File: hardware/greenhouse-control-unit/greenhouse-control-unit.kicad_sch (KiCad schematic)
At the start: 76 parts, among them J1 Pluggable_Terminal_01x02, J10 Molex_KK-396_01x16, J10_LittleBuck1 Conn_01x01_Female, J11 Molex_KK-254_01x10, J11_LittleBuck1 Conn_01x01_Female, J12_BigBuck1 Conn_01x01_Female, J13_BigBuck1 Conn_01x01_Female, J14_LittleBuck1 Conn_01x01_Female, J15_LittleBuck1 Conn_01x01_Female, J2 Pluggable_Terminal_01x02, J3 Pluggable_Terminal_01x02, J4 Pluggable_Terminal_01x02, J5 Molex_KK-254_01x08, J6 Conn_01x10_Female, J6_BigBuck1 Conn_01x01_Female, J7 Conn_01x10_Female, J7_BigBuck1 Conn_01x01_Female, J8 Conn_01x15_Female, J9 Conn_01x15_Female, Q1 2N7000, Q10 IRLB8721PBF, Q11 IRLB8721PBF, Q2 2N7000, Q3 2N2222A, Q4 IRLB8721PBF, Q5 IRLB8721PBF, Q6 IRLB8721PBF, Q7 IRLB8721PBF, Q8 IRLB8721PBF, Q9 IRLB8721PBF, U1 74HC595, U2 74HC595

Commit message: Remove small buck
Also:
- Change source to 10V
- Use 5V for radios
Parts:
- removed J10_LittleBuck1, J11_LittleBuck1, J14_LittleBuck1, J15_LittleBuck1: Conn_01x01_Female, Connector_PinHeader_2.54mm:PinHeader_1x01_P2.54mm_Vertical, symbol Connector:Conn_01x01_Female
- D2: symbol Device:D_Schottky -> Device:D
- J12: renamed from J12_BigBuck1; value Conn_01x01_Female -> Buck_Conn_01x01_Female
- J13: renamed from J13_BigBuck1; value Conn_01x01_Female -> Buck_Conn_01x01_Female
- J6: renamed from J6_BigBuck1; value Conn_01x01_Female -> Buck_Conn_01x01_Female
- J7: renamed from J7_BigBuck1; value Conn_01x01_Female -> Buck_Conn_01x01_Female
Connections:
- net +5VA is gone; now on net +5V: D7.2 (A), J8.1 (Pin_1)
- net +3V3: no longer J?.2 (Pin_2), J?.4 (Pin_4)
- net +5V: now also J?.2 (Pin_2), J?.4 (Pin_4)
- net +12V renamed +10V
- net Batt+12V renamed Batt+10V
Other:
- note added: "Prototype TODO: -"
- note added: "Schematic TODO: - Disable SR when no input voltage (SR can draw power from inputs; i.e. MC) - Consider adding reverse voltage protection to power outputs - Check if PSU relay module has flyback diode"
- note removed: "Prototype TODO: - Add reverse voltage protection diode to battery relay - Check all R values - Test current on each SR out (max 20mA, limit 35mA) - Test current on SR VCC (max 70mA)"
- note removed: "Schematic TODO: - Disable SR when no input voltage (SR can draw power from inputs; i.e. MC) - Consider adding reverse voltage protection to power outputs - Check if PSU relay module has reverse voltage diode"
- moved on the sheet: H1, H2, H3, H4, H5, H6, J12, J13, J6, J7

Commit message: Reconfigured SR OE
Also:
- merged motor driver back into main schematic (to avoid needing global labels)
- renamed labels for headers/sockets
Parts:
- removed C1, C2: 0.01 μf, Capacitor_THT:C_Disc_D3.0mm_W1.6mm_P2.50mm, symbol Device:C
- removed D7: 1N4001, Diode_THT:D_DO-41_SOD81_P10.16mm_Horizontal, symbol Diode:1N4001
- removed J?: TX_PinHeader_1x04_P2.54mm, Connector_Molex:Molex_KK-254_AE-6410-08A_1x04_P2.54mm_Vertical, symbol Connector:Conn_01x04_Female
- removed J?: RX_PinHeader_1x04_P2.54mm, Connector_PinHeader_2.54mm:PinHeader_1x04_P2.54mm_Vertical, symbol Connector:Conn_01x04_Female
- removed Q?: 2N2222A, Package_TO_SOT_THT:TO-92_Inline, symbol Nick:2N2222A
- removed R9: 10k, Resistor_THT:R_Axial_DIN0204_L3.6mm_D1.6mm_P5.08mm_Horizontal, symbol Device:R
- removed R?: 100k, Resistor_THT:R_Axial_DIN0207_L6.3mm_D2.5mm_P7.62mm_Horizontal, symbol Device:R
- added C1, C2: 0.01 μf, Capacitor_THT:C_Disc_D3.0mm_W1.6mm_P2.50mm, symbol Device:C_Small
- added C3, C4: 100nF, Capacitor_THT:C_Disc_D4.7mm_W2.5mm_P5.00mm, symbol Device:C_Small
- added D11, D12, D13, D14, D15, D16, D17, D18: 1N4007, Diode_THT:D_DO-41_SOD81_P10.16mm_Horizontal, symbol Diode:1N4007
- added D4: 1N4001, Diode_THT:D_DO-41_SOD81_P10.16mm_Horizontal, symbol Device:D
- added D8: 1N4001, Diode_THT:D_DO-41_SOD81_P10.16mm_Horizontal, symbol Diode:1N4001
- added J?: Conn_01x03_Male, symbol Connector:Conn_01x03_Male
- added J?: RX_PinHeader_1x04_P2.54mm, Connector_PinHeader_2.54mm:PinHeader_1x04_P2.54mm_Vertical, symbol Connector:Conn_01x04_Female
- added J?: TX_PinHeader_1x04_P2.54mm, Connector_PinHeader_2.54mm:PinHeader_1x04_P2.54mm_Vertical, symbol Connector:Conn_01x04_Female
- added Q4, Q5: 2N2222A, Package_TO_SOT_THT:TO-92_Inline, symbol Nick:2N2222A
- added R10, R14, R15, R26, R7: 10k, Resistor_THT:R_Axial_DIN0207_L6.3mm_D2.5mm_P7.62mm_Horizontal, symbol Device:R
- added R17: 10k, Resistor_THT:R_Axial_DIN0204_L3.6mm_D1.6mm_P5.08mm_Horizontal, symbol Device:R
- added U3: L298HN, Package_TO_SOT_THT:TO-220-15_P2.54x2.54mm_StaggerOdd_Lead4.58mm_Vertical, symbol Driver_Motor:L298HN
- gave numbers to parts that had none: 1
- renumbered D9 to D10, D4 to D5, D5 to D6, D6 to D7, D8 to D9, J8 to J10, J6 to J11, J7 to J12, J9 to J13, J10 to J16, J11 to J17, J12 to J8, J13 to J9, Q8 to Q10, Q9 to Q11, Q10 to Q12, Q11 to Q13, Q4 to Q6, Q5 to Q7, Q6 to Q8, Q7 to Q9, R10 to R11, R11 to R12, R12 to R13, R17 to R16, R13 to R18, R14 to R19, R15 to R20, R16 to R21, R18 to R22, R19 to R23, R20 to R24, R21 to R25, R7 to R9
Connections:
- net +10V: now also C4.1, D11.1 (K), D13.1 (K), D15.1 (K), D17.1 (K), U3.9 (Vss); no longer J5.1 (Pin_1)
- net +5V: now also J5.1 (Pin_1), U2.7 (QH), C3.2, D4.2 (A), D8.2 (A), J?.1 (Pin_1), J?.1 (Pin_1), J?.2 (Pin_2), J?.4 (Pin_4), R14.1, R26.1, U3.11 (EnB), U3.4 (Vs), U3.6 (EnA); no longer J10.1 (Pin_1), J5.2 (Pin_2)
- net BattRelayNC_SR_Q0: now also R7.2
- net CaseFan_SR_Q2: now also R10.2
- net GND: now also D6.1 (K), J5.2 (Pin_2), Q2.3 (D), C1.1, C2.1, C3.1, C4.2, D12.2 (A), D14.2 (A), D16.2 (A), D18.2 (A), J?.2 (Pin_2), J?.4 (Pin_4), Q4.1 (E), Q5.1 (E), R10.1, R7.1, U3.1 (SENSE_A), U3.15 (SENSE_B), U3.8 (GND); no longer J5.3 (Pin_3), U1.8 (GND), U2.8 (GND)
- net MC_D0: now also J?.2 (Pin_2), J?.3 (Pin_3)
- net MC_D8: now also R15.1; no longer U2.13 (~{OE})
- net Motor1_SR_Q6: now also U3.10 (IN3), U3.5 (IN1); no longer J5.7 (Pin_7)
- net Motor2_SR_Q7: now also U3.12 (IN4), U3.7 (IN2); no longer J5.8 (Pin_8)
- net PsuRelayNC_Coil: now also J?.3 (Pin_3); no longer J5.5 (Pin_5)
- net SR_CLR: now also C1.2, C2.2, D8.1 (K), R17.1
- net SR_QH1: now reaches U1.9 (QH'), U2.14 (SER)
- net SR_OE: now reaches U1.13 (~{OE})
- net SR_OE: now also U2.13 (~{OE}), Q5.3 (C), R17.2
- net RAD_TX_GND: now reaches Q14.3 (C)
- net RAD_TX_GND: now also J?.3 (Pin_3)
- net Motor1_OutB: now reaches J5.4 (Pin_4)
- net Motor1_OutB: now also D13.2 (A), D14.1 (K), U3.3 (OUT2)
- removed net CaseFan_FET: D6.1 (K), J5.6 (Pin_6), Q2.3 (D)
- net RAD_TX_EN: no longer names the net of Q14.2 (B)
- net RAD_TX_EN: now also R26.2; no longer U2.7 (QH)
- new net: D4.1 (K), J10.1 (Pin_1)
- new net: Q5.2 (B), R15.2
- new net: Q4.2 (B), R14.2
- new net Motor1_OutA: D11.2 (A), D12.1 (K), J5.3 (Pin_3), U3.2 (OUT1)
- new net Motor2_OutA: D15.2 (A), D16.1 (K), J5.5 (Pin_5), U3.13 (OUT3)
- new net Motor2_OutB: D17.2 (A), D18.1 (K), J5.6 (Pin_6), U3.14 (OUT4)
- new net RAD_TX_DATA: J?.1 (Pin_1)
- new net SR_GND: Q4.3 (C), U1.8 (GND), U2.8 (GND)
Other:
- removed sheet L298N motor driver
- note added: "Flyback diodes"
- note added: "Invert SR OE, as D8 can't be high at boot"
- note added: "Prevent MCU from powering SR via inputs"
- note added: "TODO: Figure out why these are FETs instead of BJTs"
- moved on the sheet: BZ1, D1, D10, D3, D5, D6, D7, D9, J10, J11, J12, J13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

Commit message: Cleanup TODOs
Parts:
- J18: renamed from J?; footprint (none) -> Connector_PinHeader_2.54mm:PinHeader_1x03_P2.54mm_Vertical
- gave numbers to parts that had none: 2
- renumbered D7 to D1, D11 to D10, D12 to D11, D6 to D12, D1 to D2, D2 to D3, D9 to D4, D3 to D5, D4 to D6, D10 to D7, D5 to D8, D8 to D9, J6 to J1, J12 to J10, J10 to J11, J13 to J12, J16 to J13, J17 to J14, J5 to J17, J7 to J2, J8 to J3, J9 to J4, J1 to J5, J2 to J6, J3 to J7, J4 to J8, J11 to J9, Q3 to Q1, Q1 to Q2, Q2 to Q3, R8 to R10, R6 to R11, R7 to R12, R9 to R13, R10 to R14, R14 to R15, R15 to R16, R11 to R3, R12 to R4, R3 to R5, R4 to R6, R13 to R7, R5 to R8, R16 to R9, U3 to U1, U1 to U2, U2 to U3
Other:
- note added: "Schematic TODO: - Prototype TODO: - PCB TODO: -"
- note removed: "PCB TODO: -"
- note removed: "Prototype TODO: -"
- note removed: "Schematic TODO: - Disable SR when no input voltage (SR can draw power from inputs; i.e. MC) - Consider adding reverse voltage protection to power outputs - Check if PSU relay module has flyback diode"

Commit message: Removed PSU separation + voltage sensor
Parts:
- removed D2: DSB20I15PA Schottky, Package_TO_SOT_THT:TO-220-2_Vertical, symbol Device:D_Schottky
- removed D3: 1N4001, Diode_THT:D_DO-41_SOD81_P10.16mm_Horizontal, symbol Device:D
- removed J9: Conn_01x10_Female, Connector_PinSocket_2.54mm:PinSocket_1x10_P2.54mm_Vertical, symbol Connector:Conn_01x10_Female
- removed Q4: 2N2222A, Package_TO_SOT_THT:TO-92_Inline, symbol Nick:2N2222A
- removed R1: 4k6, Resistor_THT:R_Axial_DIN0207_L6.3mm_D2.5mm_P7.62mm_Horizontal, symbol Device:R
- removed R15: 10k, Resistor_THT:R_Axial_DIN0207_L6.3mm_D2.5mm_P7.62mm_Horizontal, symbol Device:R
- removed R2: 1k, Resistor_THT:R_Axial_DIN0207_L6.3mm_D2.5mm_P7.62mm_Horizontal, symbol Device:R
- added D8: 1N4001, Diode_THT:D_DO-41_SOD81_P10.16mm_Horizontal, symbol Device:D
- D6: Field4 (none) -> Flyback
- R5: value 4k6 -> 1M
- R6: value 1k -> 220k
- renumbered D4 to D3, D5 to D4, D7 to D5, D8 to D7, Q11 to Q10, Q12 to Q11, Q13 to Q12, Q14 to Q13, Q5 to Q4, Q6 to Q5, Q7 to Q6, Q8 to Q7, Q9 to Q8, Q10 to Q9, R16 to R15, R17 to R16, R18 to R17, R19 to R18, R20 to R19, R21 to R20, R22 to R21, R23 to R22, R24 to R23, R25 to R24, R26 to R25
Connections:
- net BattRelayNC_Coil_A is gone; now on net +10V: J5.1 (Pin_1), J8.1 (Pin_1)
- net SR_GND is gone; now on net GND: U2.8 (GND), U3.8 (GND)
- net +10V: now also D6.1 (K)
- net +5V: now also J11.1 (Pin_1); no longer D6.2 (A)
- net BattRelayNC_Coil_B: now also D6.2 (A), D8.2 (A); no longer D7.1 (K), Q2.3 (D)
- net GND: now also J10.5 (Pin_5)
- net MC_D8: now also U3.13 (~{OE})
- net ADC1_SCA renamed ADC2_SCA
- net ADC2_SCA: no longer J10.5 (Pin_5)
- net ADC1_SCL renamed ADC2_SCL
- net SR_OE renamed SR_~{OE}
- net SR_~{OE}: no longer U3.13 (~{OE})
- new net: D7.1 (K), D8.1 (K), Q2.3 (D)
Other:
- note added: "D8 is needed to stop D7 current flowing back through D6 to PSU+10V"
- note added: "Invert SR_~{OE}, as D8 can't be high at boot"
- note removed: "Invert SR OE, as D8 can't be high at boot"
- note removed: "Prevent MCU from powering SR via inputs"
- moved on the sheet: BZ1, D1, D3, D4, D5, D7, J7, J8, Q1, R11, R3, R4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

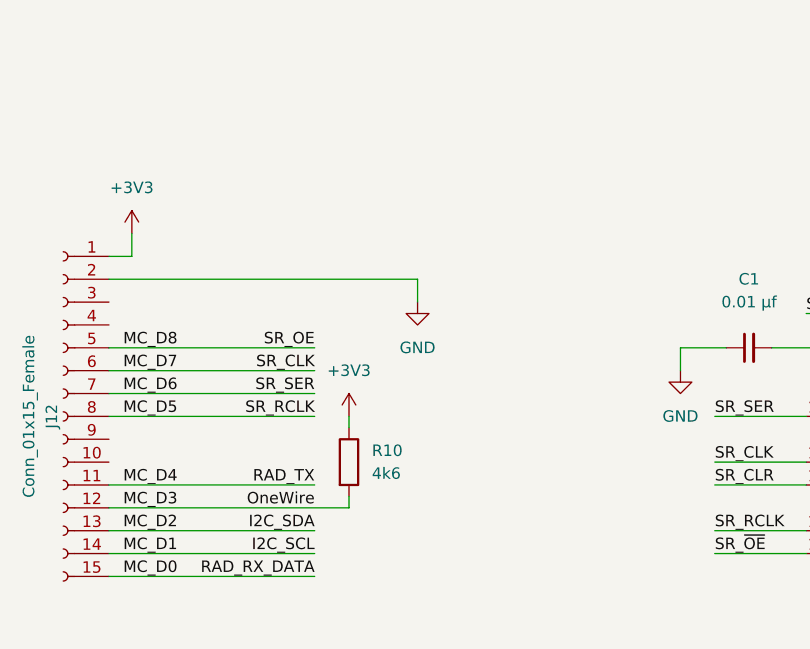
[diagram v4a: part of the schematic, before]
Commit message: Add TODO and changed label name
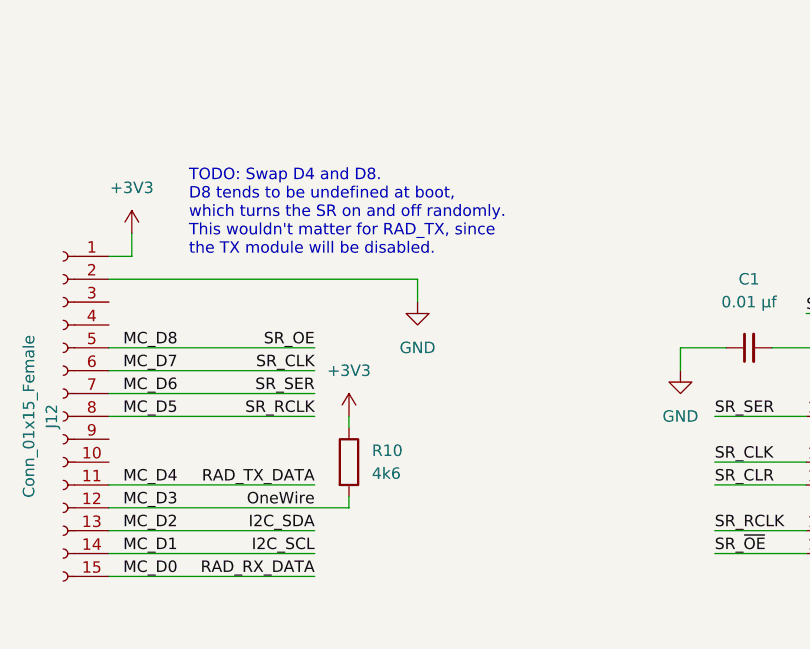
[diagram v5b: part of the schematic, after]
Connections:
- net RAD_TX_DATA is gone; now on net MC_D4: J16.1 (Pin_1)
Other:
- note added: "TODO: Swap D4 and D8. D8 tends to be undefined at boot, which turns the SR on and off randomly. This wouldn't matter for RAD_TX, since the TX module will be disabled."
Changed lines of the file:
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@@
     (stroke (width 0) (type default) (color 0 0 0 0))
+  )
+  (text "TODO: Swap D4 and D8. \nD8 tends to be undefined at boot,\nwhich turns the SR on and off randomly. \nThis wouldn't matter for RAD_TX, since\nthe TX module will be disabled."
+    (at 186.69 86.36 0)
+    (effects (font (size 1.27 1.27)) (justify left bottom))
   )
   (text "On when using battery" (at 104.14 363.22 0)
@@
     (effects (font (size 1.27 1.27)) (justify left bottom))
   )
-  (label "RAD_TX" (at 200.66 111.76 180)
-    (effects (font (size 1.27 1.27)) (justify right bottom))
-  )
+  (label "RAD_TX_DATA" (at 200.66 111.76 180)
+    (effects (font (size 1.27 1.27)) (justify right bottom))
+  )

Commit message: Restore SR OE (non-inverted)
- Swapped D5/D8; D5 for SR OE which can stay HIGH through reset (except for minor 5ms dip).
- Pull OE to +3V3 instead of +5V to protect MCU GPIO.
- Power SR from VU (+5V USB) so we can test SR without main power.
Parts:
- removed Q4: 2N2222A, Package_TO_SOT_THT:TO-92_Inline, symbol Nick:2N2222A
- removed R15: 10k, Resistor_THT:R_Axial_DIN0207_L6.3mm_D2.5mm_P7.62mm_Horizontal, symbol Device:R
- removed R16: 10k, Resistor_THT:R_Axial_DIN0204_L3.6mm_D1.6mm_P5.08mm_Horizontal, symbol Device:R
- added R?: 10k, Resistor_THT:R_Axial_DIN0207_L6.3mm_D2.5mm_P7.62mm_Horizontal, symbol Device:R
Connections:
- net MC_A0 is gone; now on net ADC1_A3: J11.15 (Pin_15)
- net SR_~{OE} is gone; now on net MC_D5: U2.13 (~{OE})
- net +3V3: now also J15.1 (Pin_1), J16.2 (Pin_2), J16.4 (Pin_4), R?.1
- net +5V: no longer J15.1 (Pin_1), J16.2 (Pin_2), J16.4 (Pin_4), R25.1, U3.7 (QH)
- net MC_D5: now also R?.2; no longer U2.12 (RCLK), U3.12 (RCLK)
- net MC_D7: no longer U3.11 (SRCLK)
- net MC_D8: now also U2.12 (RCLK), U3.12 (RCLK); no longer U3.13 (~{OE})
- net SR_CLR: no longer C1.2, C2.2, D9.1 (K), U2.10 (~{SRCLR}), U2.16 (VCC), U3.16 (VCC)
- net MC_VU: now reaches J11.13 (Pin_13)
- net MC_VU: now also C1.2, C2.2, D9.1 (K), U2.10 (~{SRCLR}), U2.16 (VCC), U3.16 (VCC)
- new net RAD_TX_EN: R25.1, U3.7 (QH)
- new net SR_CLK: U3.11 (SRCLK)
- new net SR_OE: U3.13 (~{OE})
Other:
- note added: "TODO: Remove D3 and use for RX/TX?"
- note removed: "Invert SR_~{OE}, as D8 can't be high at boot"
- note removed: "TODO: Swap D4 and D8. D8 tends to be undefined at boot, which turns the SR on and off randomly. This wouldn't matter for RAD_TX, since the TX module will be disabled."
- moved on the sheet: BZ1, D1, D3, D4, D5, J10, Q1, R3, R4, R5, R6, R7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

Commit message: Change LEDs to current sink (PCB WIP)
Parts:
- removed C3, C4: 100nF, Capacitor_THT:C_Disc_D4.7mm_W2.5mm_P5.00mm, symbol Device:C_Small
- removed D10, D11, D13, D14, D15, D16, D17, D18: 1N4007, Diode_THT:D_DO-41_SOD81_P10.16mm_Horizontal, symbol Diode:1N4007
- removed U1: L298HN, Package_TO_SOT_THT:TO-220-15_P2.54x2.54mm_StaggerOdd_Lead4.58mm_Vertical, symbol Driver_Motor:L298HN
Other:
- note removed: "Flyback diodes"
- moved on the sheet: BZ1, C1, C2, D1, D12, D3, D4, D5, D6, D7, D8, D9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

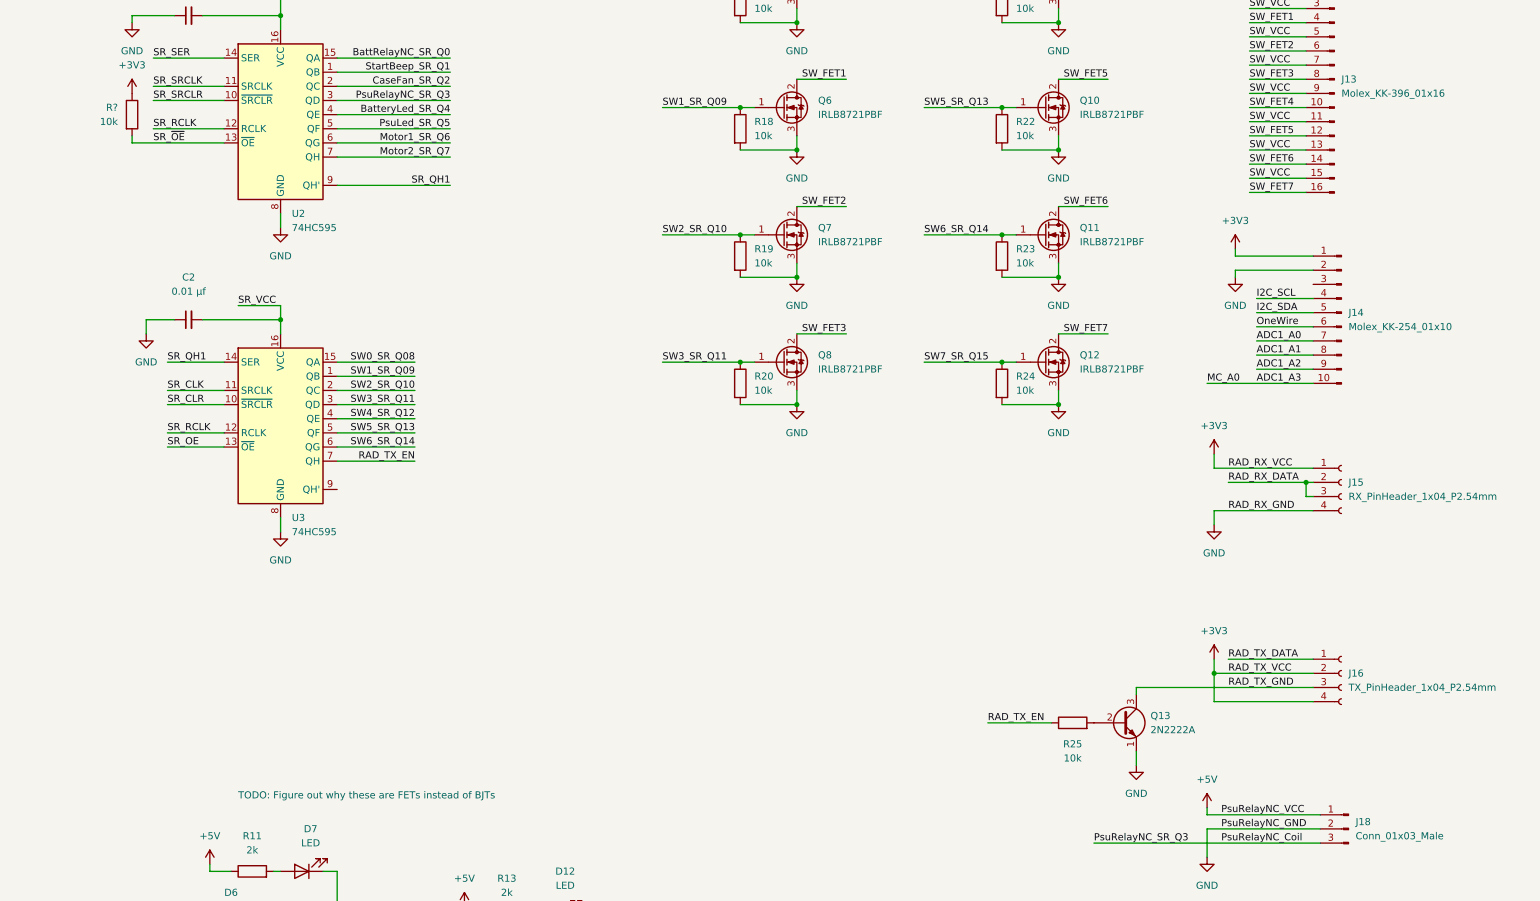
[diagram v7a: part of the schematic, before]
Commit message: Replace RX/TX modules with HC-12
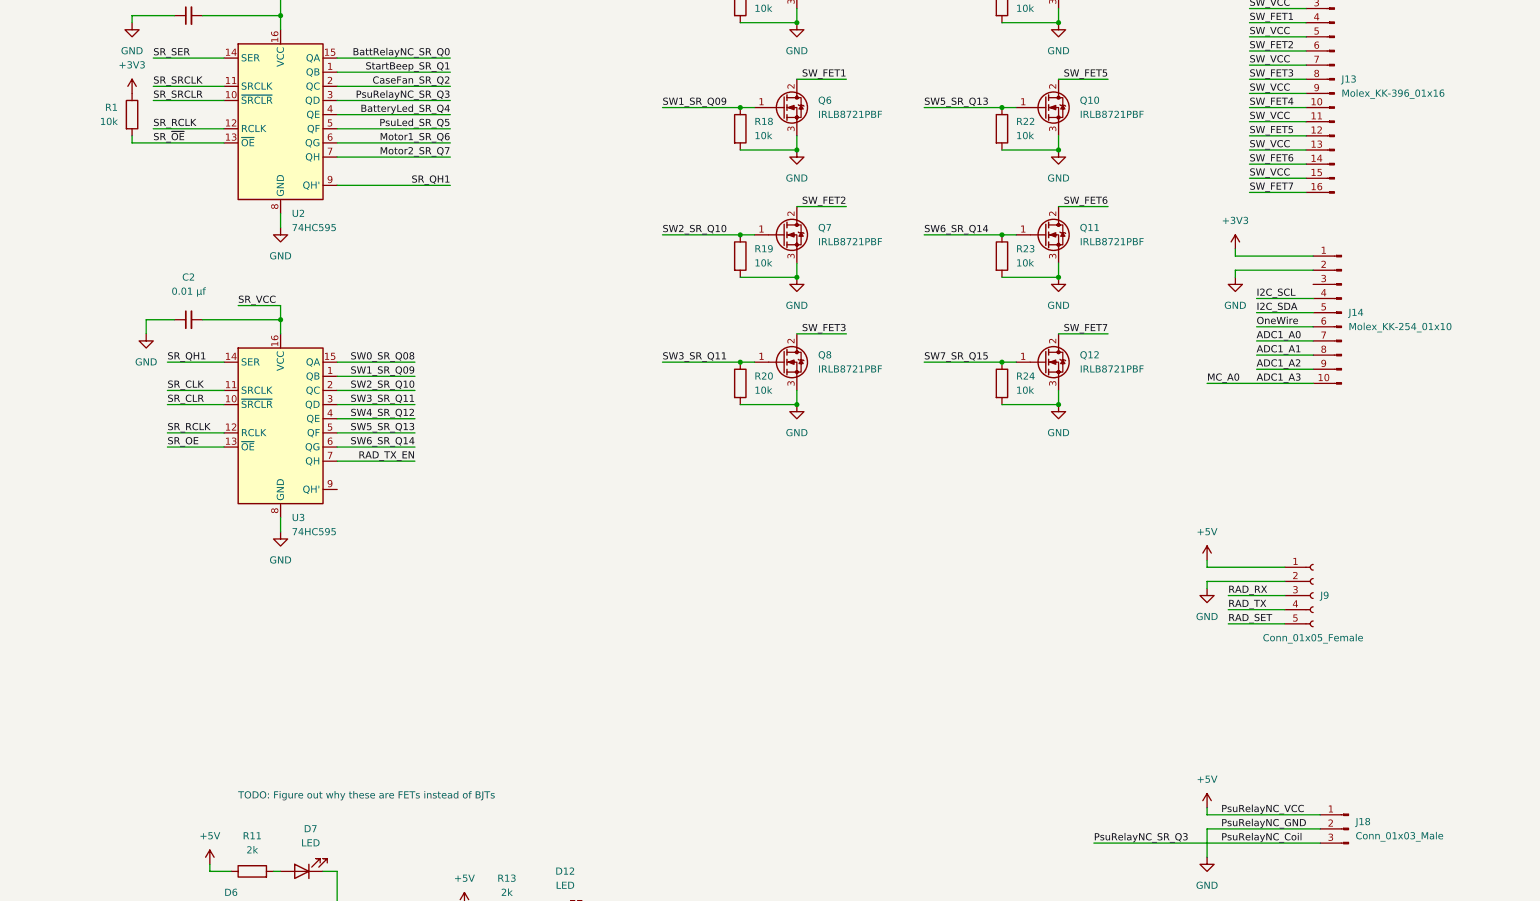
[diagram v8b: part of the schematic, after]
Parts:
- removed J15: RX_PinHeader_1x04_P2.54mm, Connector_PinHeader_2.54mm:PinHeader_1x04_P2.54mm_Vertical, symbol Connector:Conn_01x04_Female
- removed J16: TX_PinHeader_1x04_P2.54mm, Connector_PinHeader_2.54mm:PinHeader_1x04_P2.54mm_Vertical, symbol Connector:Conn_01x04_Female
- removed Q13: 2N2222A, Package_TO_SOT_THT:TO-92_Inline, symbol Nick:2N2222A
- removed R25: 10k, Resistor_THT:R_Axial_DIN0207_L6.3mm_D2.5mm_P7.62mm_Horizontal, symbol Device:R
- added J9: Conn_01x05_Female, Connector_PinSocket_2.54mm:PinSocket_1x05_P2.54mm_Vertical, symbol Connector:Conn_01x05_Female
- gave numbers to parts that had none: 1
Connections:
- net +5V: now also J9.1 (Pin_1)
- net GND: now also J9.2 (Pin_2)
- new net RAD_RX: J9.3 (Pin_3)
- new net RAD_SET: J9.5 (Pin_5)
- new net RAD_TX: J9.4 (Pin_4)
